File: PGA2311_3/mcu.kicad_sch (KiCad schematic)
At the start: 86 parts, among them J301 Conn_01x16, J302 1, J303 Conn_01x02, J304 4, J305 4, Q301 BC817-40, SW301 SW_Push, SW302 Encoder PEC11R, U301 TPS60403DBV, U302 WH1602B, U303 SN74LVC8T245DW, U304 STM32G070KBT6, U305 TLV1117-50IDC, U306 LP2985-33DBV, U307 SN74LVC2G17DBV

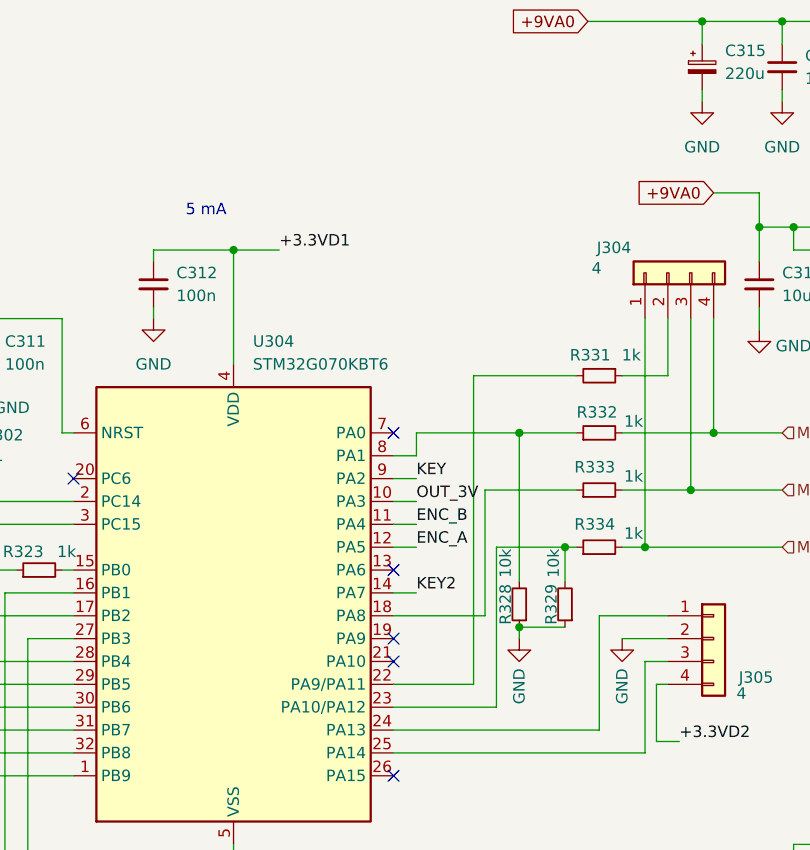
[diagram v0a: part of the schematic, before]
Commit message: Add files via upload
added pull-up resistor for CS lines
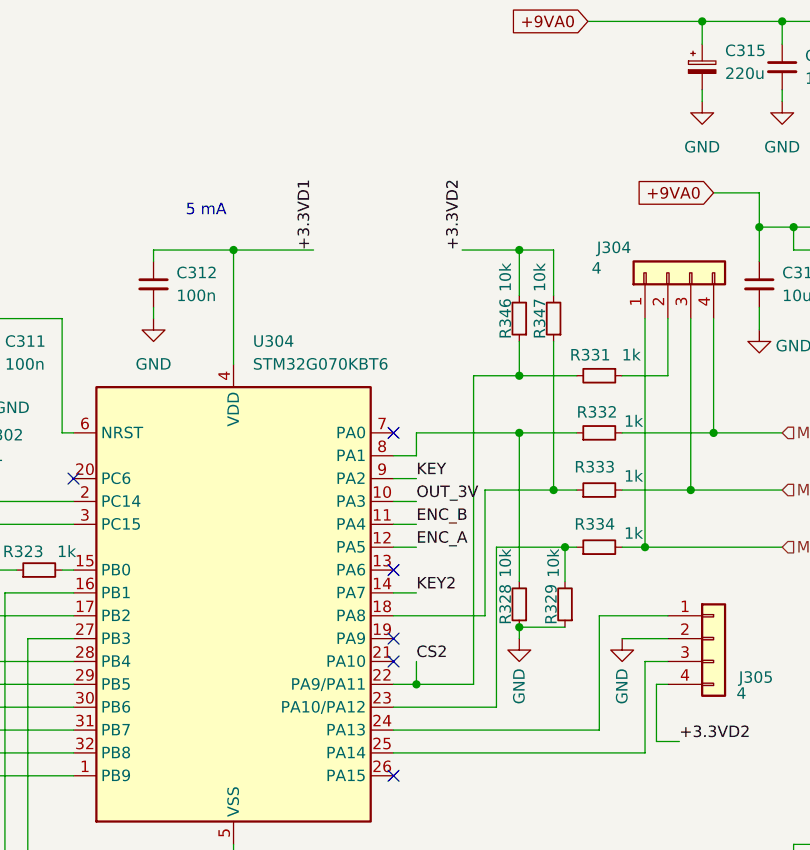
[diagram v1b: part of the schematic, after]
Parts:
- added R346, R347: 10k, Resistor_SMD:R_0805_2012Metric_Pad1.20x1.40mm_HandSolder, symbol Device:R_Small
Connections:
- net +3.3VD2: now also R346.2, R347.2
- net CS2: now reaches R331.2, U304.22 (PA9/PA11)
- net CS2: now also R346.1
- net at R333.1, U304.18 (PA8): now also R347.1

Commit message: Add files via upload
SPI connector changed to 5-pin
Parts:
- J304: footprint Connector_PinHeader_2.54mm:PinHeader_1x04_P2.54mm_Vertical -> Connector_PinHeader_2.54mm:PinHeader_1x05_P2.54mm_Vertical; symbol Connector_Generic:Conn_01x04 -> Connector_Generic:Conn_01x05
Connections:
- net GND: now also J304.1 (Pin_1)
- net MCU_CS: now also J304.4 (Pin_4); no longer J304.3 (Pin_3)
- net MCU_MOSI: now also J304.2 (Pin_2); no longer J304.1 (Pin_1)
- net MCU_SCLK: now also J304.5 (Pin_5); no longer J304.4 (Pin_4)
- net at R331.1: now also J304.3 (Pin_3); no longer J304.2 (Pin_2)
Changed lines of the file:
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@@
 	(wire
 		(pts
-			(xy 213.36 54.61) (xy 213.36 73.66)
+			(xy 213.36 53.34) (xy 213.36 73.66)
 		)
 		(stroke
@@
 	(wire
 		(pts
-			(xy 208.28 54.61) (xy 208.28 80.01)
+			(xy 208.28 53.34) (xy 208.28 80.01)
 		)
 		(stroke
@@
 	(wire
 		(pts
-			(xy 210.82 60.96) (xy 210.82 54.61)
+			(xy 210.82 60.96) (xy 210.82 53.34)
 		)
 		(stroke
@@
 	(wire
 		(pts
+			(xy 205.74 53.34) (xy 205.74 54.61)
+		)
+		(stroke
+			(width 0)
+			(type default)
+		)
+	)
+	(wire
+		(pts
 			(xy 180.34 85.09) (xy 182.88 85.09)
 		)
@@
 	(wire
 		(pts
-			(xy 215.9 54.61) (xy 215.9 67.31)
+			(xy 215.9 53.34) (xy 215.9 67.31)
 		)
 		(stroke
@@
 	)
 	(symbol
-		(lib_id "Connector_Generic:Conn_01x04")
-		(at 210.82 49.53 90)
+		(lib_id "Connector_Generic:Conn_01x05")
+		(at 210.82 48.26 90)
 		(unit 1)
 		(exclude_from_sim no)
@@
 		(dnp no)
 		(property "Reference" "J304"
-			(at 206.756 46.736 90)
+			(at 206.756 45.466 90)
 			(effects
 				(font
@@
 		)
 		(property "Value" "4"
-			(at 203.454 49.022 90)
+			(at 203.454 47.752 90)
 			(effects
 				(font
@@
 			)
 		)
-		(property "Footprint" "Connector_PinHeader_2.54mm:PinHeader_1x04_P2.54mm_Vertical"
-			(at 210.82 49.53 0)
+		(property "Footprint" "Connector_PinHeader_2.54mm:PinHeader_1x05_P2.54mm_Vertical"
+			(at 210.82 48.26 0)
 			(effects
 				(font
@@
 		)
 		(property "Datasheet" "~"
-			(at 210.82 49.53 0)
+			(at 210.82 48.26 0)
 			(effects
 				(font
@@
 			)
 		)
-		(property "Description" "Generic connector, single row, 01x04, script generated (kicad-library-utils/schlib/autogen/connector/)"
-			(at 210.82 49.53 0)
+		(property "Description" "Generic connector, single row, 01x05, script generated (kicad-library-utils/schlib/autogen/connector/)"
+			(at 210.82 48.26 0)
 			(effects
 				(font
@@
 		(pin "3"
 		)
+		(pin "5"
+		)
 		(instances
 			(project "PGA2311_3"
@@
 					(unit 1)
 				)
+			)
+		)
+	)
+	(symbol
+		(lib_id "power:GND")
+		(at 205.74 54.61 0)
+		(unit 1)
+		(exclude_from_sim no)
+		(in_bom yes)
+		(on_board yes)
+		(dnp no)
+		(property "Reference" "#PWR0319"
+			(at 205.74 60.96 0)
+			(effects
+				(font
+					(size 1.27 1.27)
+				)
+				(hide yes)
+			)
+		)
+		(property "Value" "GND"
+			(at 202.692 55.118 0)
+			(effects
+				(font
+					(size 1.27 1.27)
+				)
+			)
+		)
+		(property "Footprint" ""
+			(at 205.74 54.61 0)
+			(effects
+				(font
+					(size 1.27 1.27)
+				)
+				(hide yes)
+			)
+		)
+		(property "Datasheet" ""
+			(at 205.74 54.61 0)
+			(effects
+				(font
+					(size 1.27 1.27)
+				)
+				(hide yes)
+			)
+		)
+		(property "Description" "Power symbol creates a global label with name \"GND\" , ground"
+			(at 205.74 54.61 0)
+			(effects
+				(font
+					(size 1.27 1.27)
+				)
+				(hide yes)
+			)
+		)
+		(pin "1"
+		)
+		(instances
+			(project "PGA2311_3"
+				(path "/e4f5d1ca-8b46-4ca2-bb25-7f237c56d603/3e7d5077-9500-4fde-ab00-4eb445791b9c"
+					(reference "#PWR0319")
+					(unit 1)
+				)

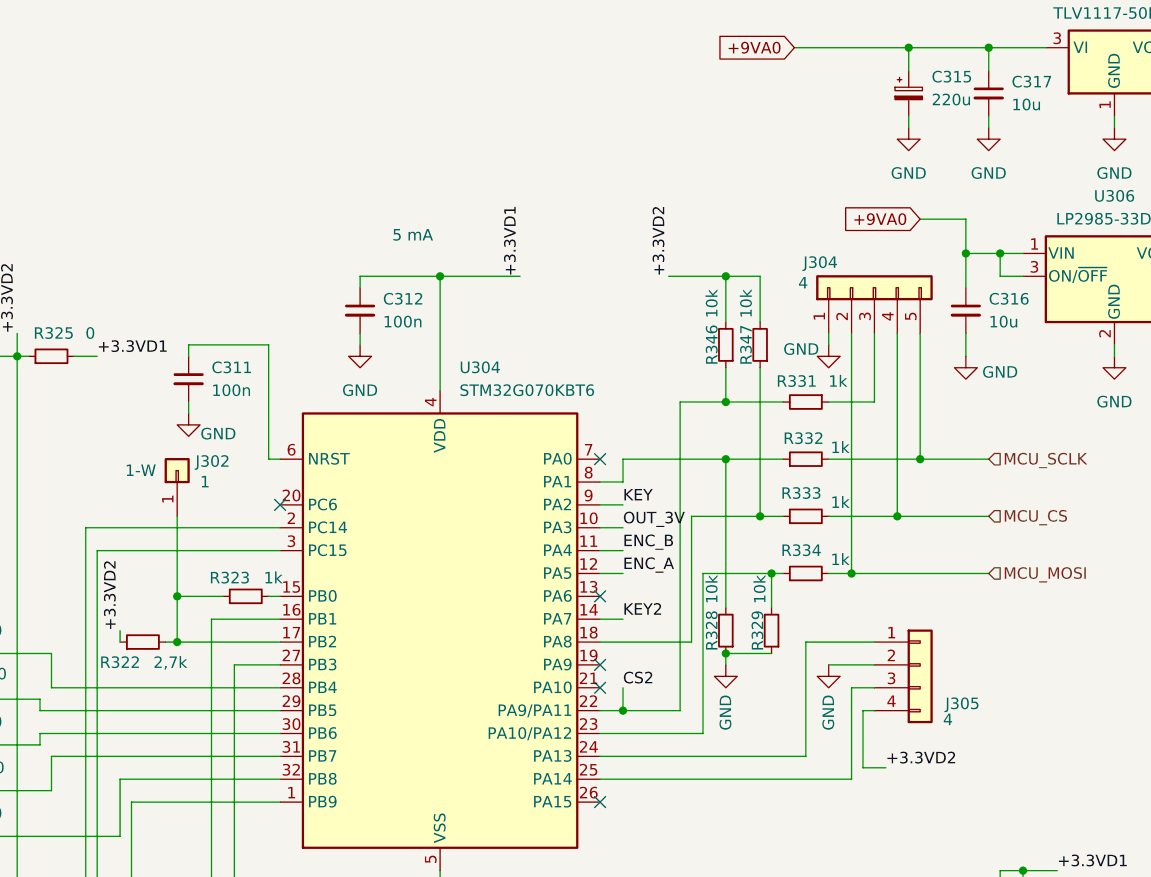
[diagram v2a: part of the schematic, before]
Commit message: Add files via upload
CS3 line added to connector
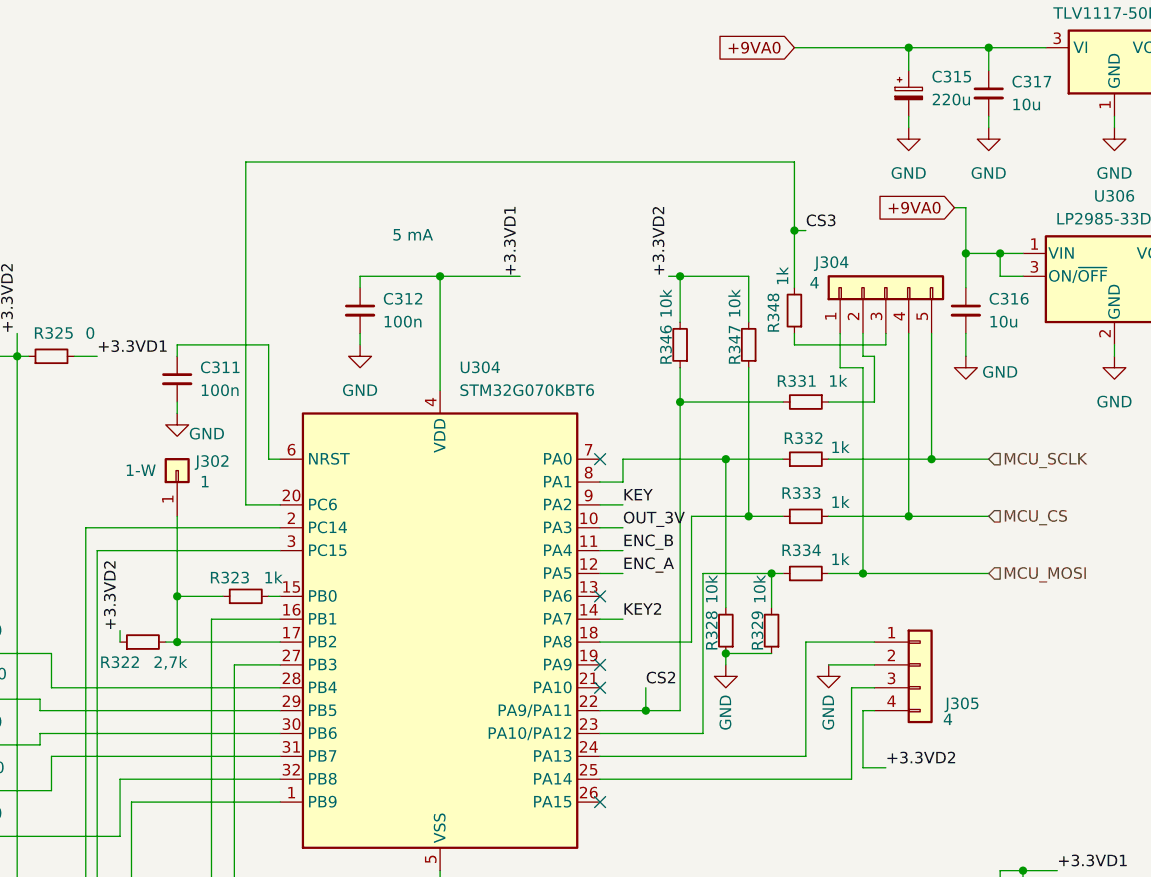
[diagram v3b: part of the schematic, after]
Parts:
- added R348: 1k, Resistor_SMD:R_0805_2012Metric_Pad1.20x1.40mm_HandSolder, symbol Device:R_Small
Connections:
- net GND: no longer J304.1 (Pin_1)
- net MCU_MOSI: now also J304.1 (Pin_1); no longer J304.2 (Pin_2)
- net at R331.1: now also J304.2 (Pin_2); no longer J304.3 (Pin_3)
- net CS3: now reaches U304.20 (PC6)
- net CS3: now also R348.2
- new net: J304.3 (Pin_3), R348.1
- no-connect marks 6 -> 5
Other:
- moved on the sheet: C311, J304, R346, R347

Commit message: Add files via upload
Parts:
- added R349: 10k, Resistor_SMD:R_0805_2012Metric_Pad1.20x1.40mm_HandSolder, symbol Device:R_Small
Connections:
- net +3.3VD2: now also R349.2
- net CS3: now also R349.1
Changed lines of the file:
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@@
 	(wire
 		(pts
+			(xy 199.39 41.91) (xy 201.93 41.91)
+		)
+		(stroke
+			(width 0)
+			(type default)
+		)
+	)
+	(wire
+		(pts
 			(xy 185.42 92.71) (xy 185.42 95.25)
 		)
@@
 	(wire
 		(pts
-			(xy 187.96 46.99) (xy 189.23 46.99)
+			(xy 181.61 46.99) (xy 189.23 46.99)
 		)
 		(stroke
@@
 	(wire
 		(pts
+			(xy 189.23 41.91) (xy 189.23 46.99)
+		)
+		(stroke
+			(width 0)
+			(type default)
+		)
+	)
+	(wire
+		(pts
 			(xy 199.39 80.01) (xy 200.66 80.01)
 		)
@@
 	(wire
 		(pts
+			(xy 194.31 41.91) (xy 189.23 41.91)
+		)
+		(stroke
+			(width 0)
+			(type default)
+		)
+	)
+	(wire
+		(pts
 			(xy 82.55 163.83) (xy 82.55 161.29)
 		)
@@
 	)
 	(label "+3.3VD2"
-		(at 187.96 46.99 90)
+		(at 181.61 46.99 90)
 		(effects
 			(font
@@
 					(unit 1)
 				)
+			)
+		)
+	)
+	(symbol
+		(lib_id "Device:R_Small")
+		(at 196.85 41.91 270)
+		(unit 1)
+		(exclude_from_sim no)
+		(in_bom yes)
+		(on_board yes)
+		(dnp no)
+		(property "Reference" "R349"
+			(at 196.85 43.434 90)
+			(effects
+				(font
+					(size 1.27 1.27)
+				)
+			)
+		)
+		(property "Value" "10k"
+			(at 192.278 43.434 90)
+			(effects
+				(font
+					(size 1.27 1.27)
+				)
+			)
+		)
+		(property "Footprint" "Resistor_SMD:R_0805_2012Metric_Pad1.20x1.40mm_HandSolder"
+			(at 196.85 41.91 0)
+			(effects
+				(font
+					(size 1.27 1.27)
+				)
+				(hide yes)
+			)
+		)
+		(property "Datasheet" "~"
+			(at 196.85 41.91 0)
+			(effects
+				(font
+					(size 1.27 1.27)
+				)
+				(hide yes)
+			)
+		)
+		(property "Description" "Resistor, small symbol"
+			(at 196.85 41.91 0)
+			(effects
+				(font
+					(size 1.27 1.27)
+				)
+				(hide yes)
+			)
+		)
+		(pin "1"
+		)
+		(pin "2"
+		)
+		(instances
+			(project "PGA2311_3"
+				(path "/e4f5d1ca-8b46-4ca2-bb25-7f237c56d603/3e7d5077-9500-4fde-ab00-4eb445791b9c"
+					(reference "R349")
+					(unit 1)
+				)
